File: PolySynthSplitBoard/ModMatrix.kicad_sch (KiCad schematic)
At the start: 89 parts, among them SW501 SB, SW502 MS1, SW503 MD1, SW504 MS2, SW505 MD2, SW506 MS3, SW507 MD3, SW508 MS4, SW509 MD4, SW510 MS5, SW511 MD5, SW512 MS6, SW513 MD6, SW514 MD7, SW515 MD8, U501 MCP23S17_SS

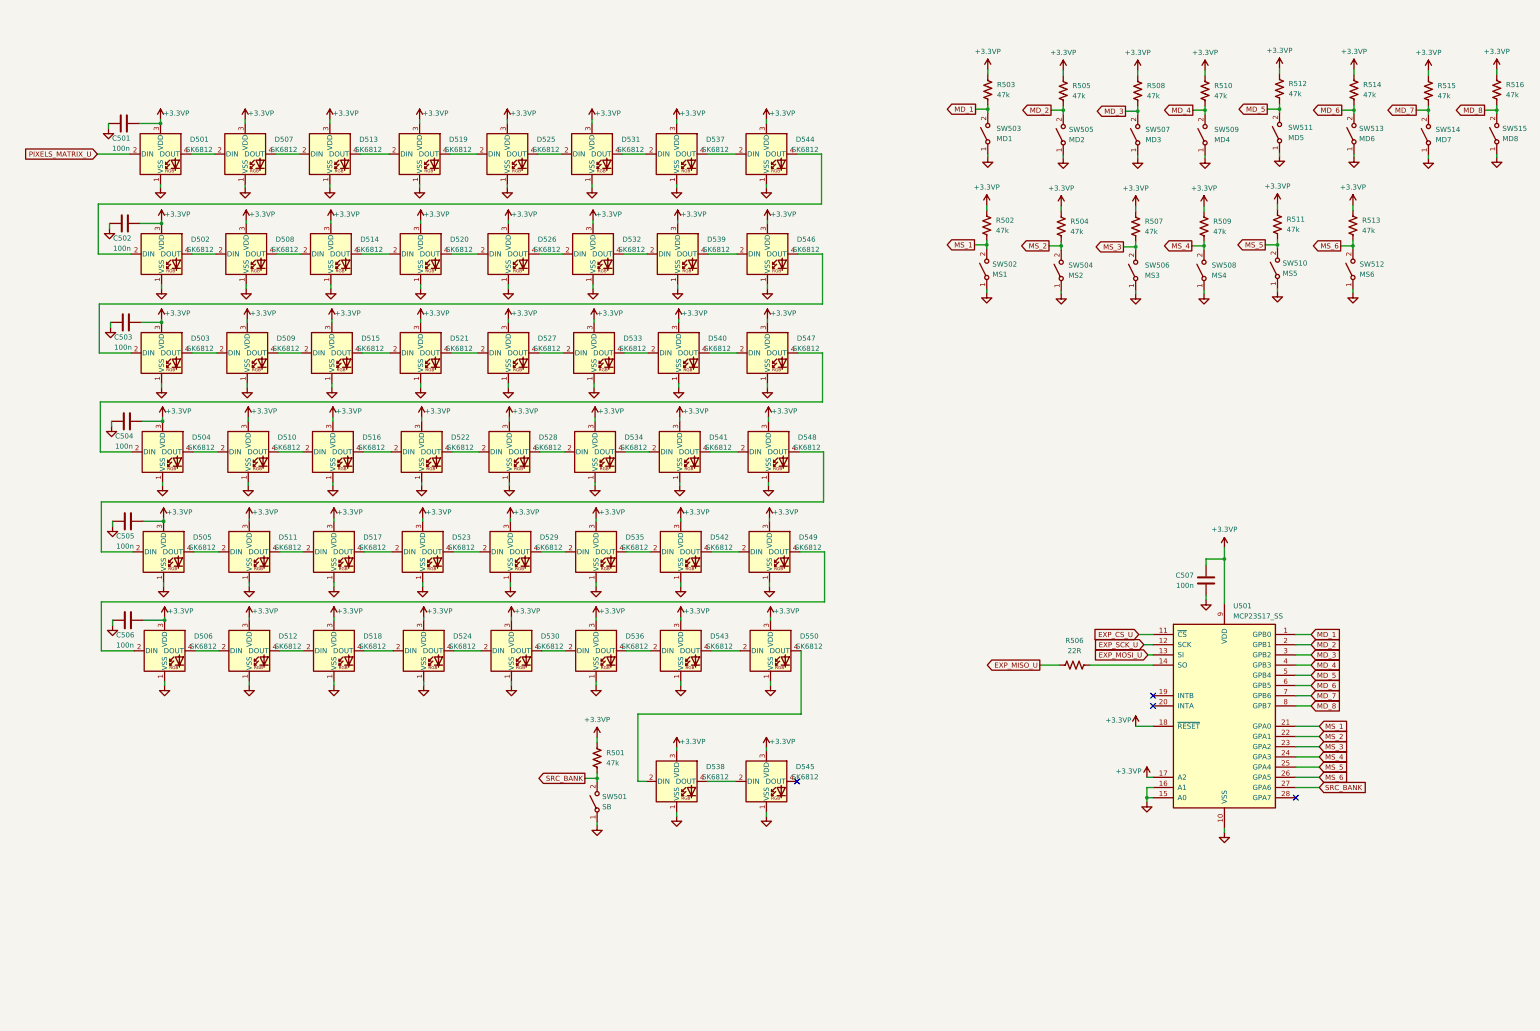
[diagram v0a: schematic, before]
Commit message: more decoupling on pixels, moved power connector
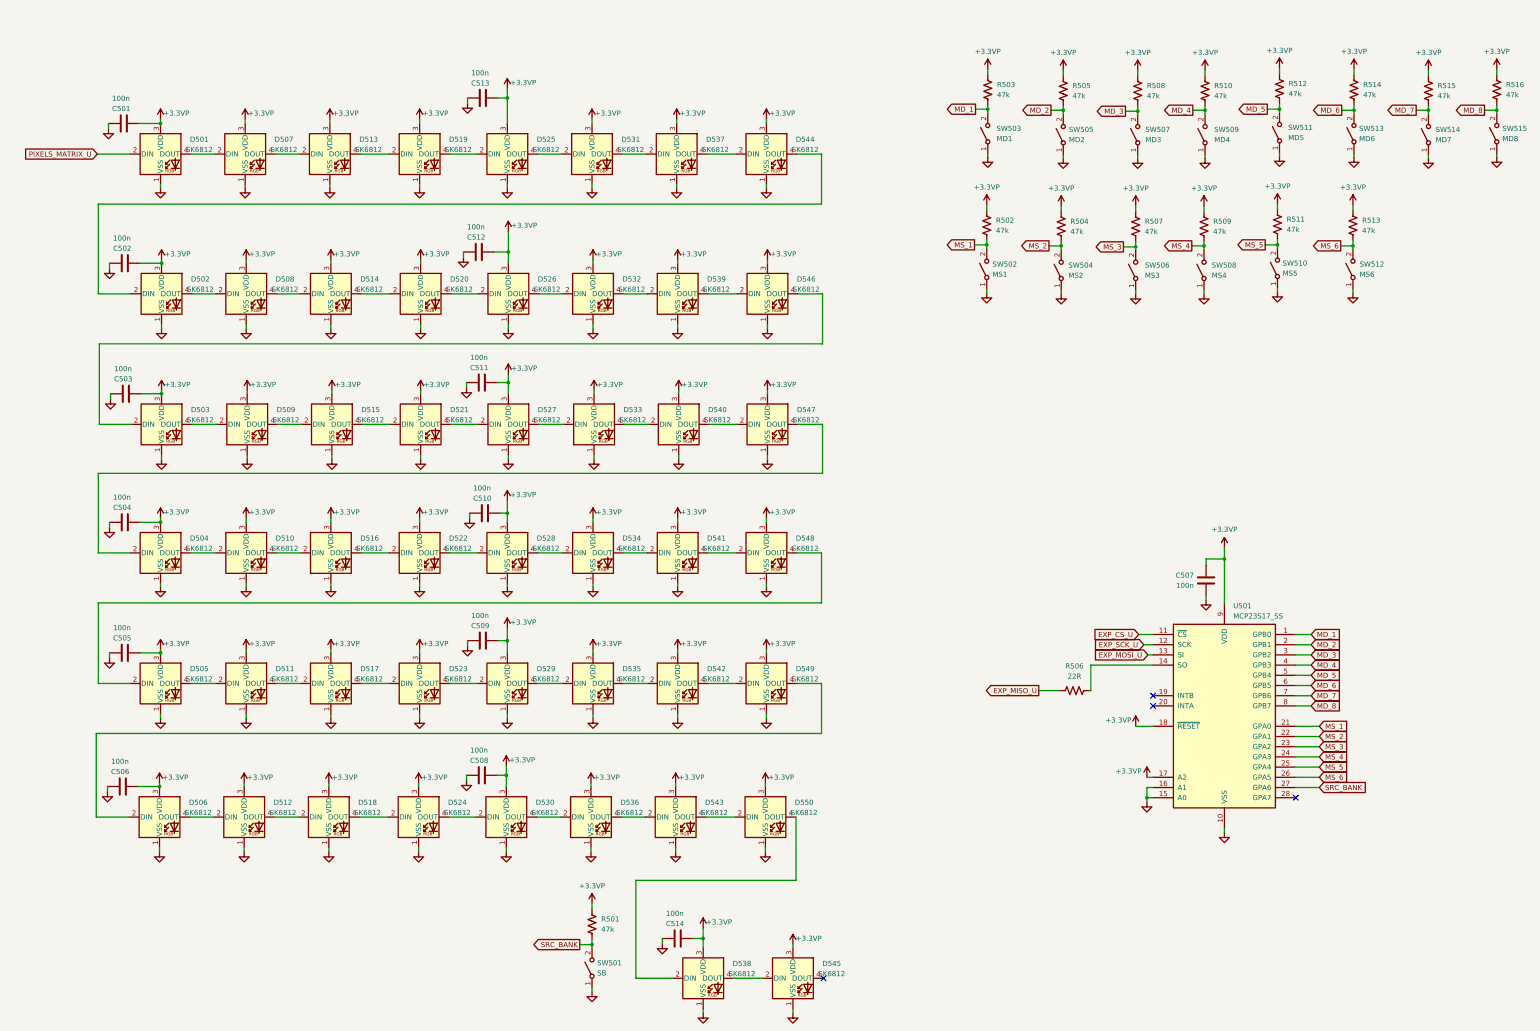
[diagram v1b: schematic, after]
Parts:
- added C508, C509, C510, C511, C512, C513, C514: 100n, Capacitor_SMD:C_0805_2012Metric, symbol Device:C
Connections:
- net +3.3VP: now also C508.2, C509.2, C510.2, C511.2, C512.2, C513.2, C514.2
- net GNDA: now also C508.1, C509.1, C510.1, C511.1, C512.1, C513.1, C514.1
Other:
- moved on the sheet: C502, C503, C504, C505, C506, D502, D503, D504, D505, D506, D508, D509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

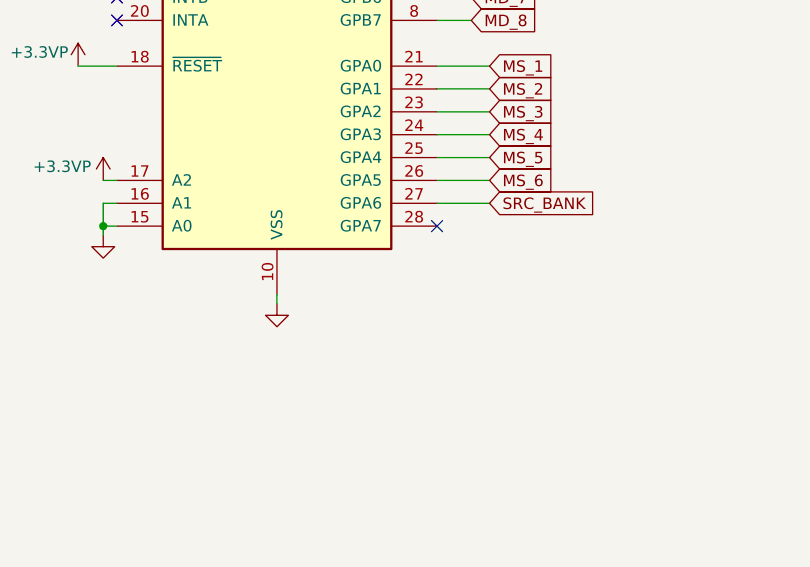
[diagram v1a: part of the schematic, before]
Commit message: Button indeces and mapping
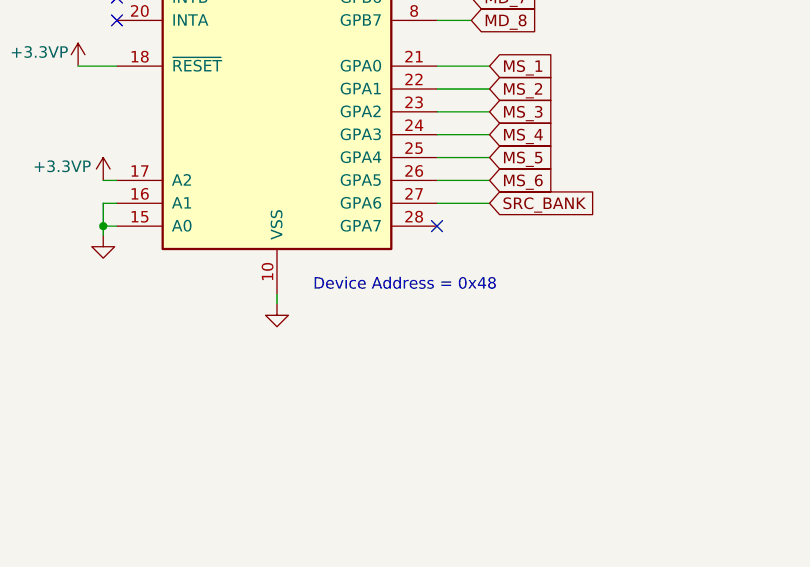
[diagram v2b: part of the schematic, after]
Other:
- note added: "Device Address = 0x48"
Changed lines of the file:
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@@
+		)
+	)
+	(text "Device Address = 0x48"
+		(exclude_from_sim no)
+		(at 335.788 223.52 0)
+		(effects
+			(font
+				(size 1.27 1.27)
+			)
 		)
 	)

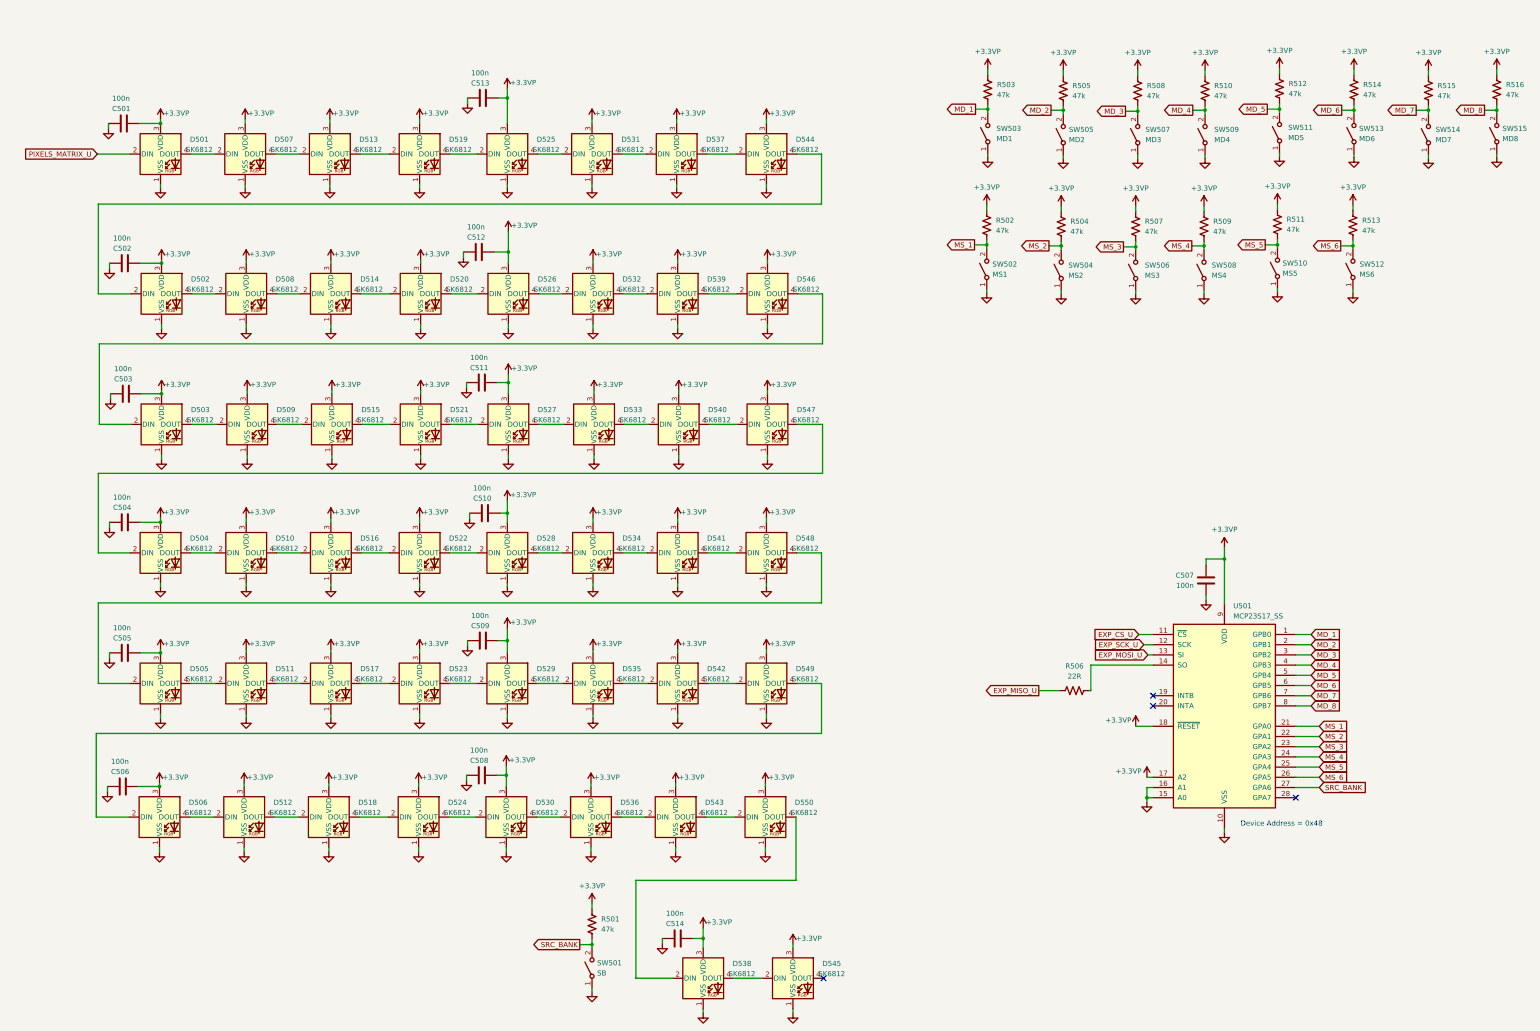
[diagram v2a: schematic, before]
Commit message: switching to 20p mezzanine connectors
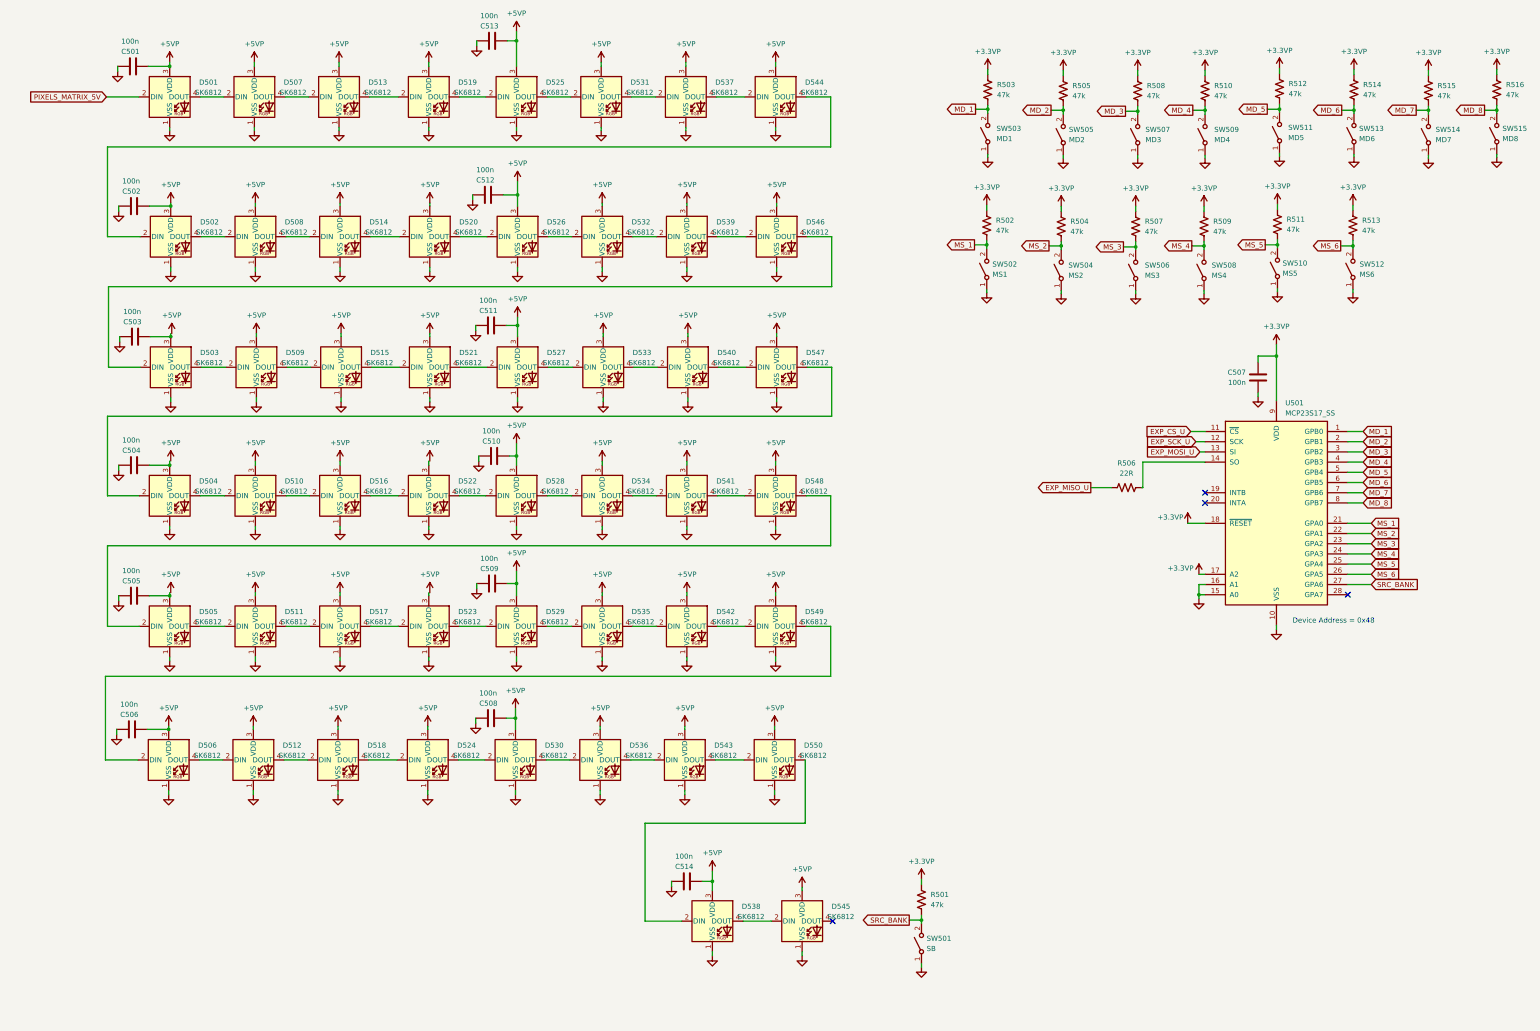
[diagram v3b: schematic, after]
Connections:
- net +3.3VP: no longer C501.2, C502.2, C503.2, C504.2, C505.2, C506.2, C508.2, C509.2, C510.2, C511.2, C512.2, C513.2, C514.2, D501.3 (VDD), D502.3 (VDD), D503.3 (VDD), D504.3 (VDD), D505.3 (VDD), D506.3 (VDD), D507.3 (VDD), D508.3 (VDD), D509.3 (VDD), D510.3 (VDD), D511.3 (VDD), D512.3 (VDD), D513.3 (VDD), D514.3 (VDD), D515.3 (VDD), D516.3 (VDD), D517.3 (VDD), D518.3 (VDD), D519.3 (VDD), D520.3 (VDD), D521.3 (VDD), D522.3 (VDD), D523.3 (VDD), D524.3 (VDD), D525.3 (VDD), D526.3 (VDD), D527.3 (VDD), D528.3 (VDD), D529.3 (VDD), D530.3 (VDD), D531.3 (VDD), D532.3 (VDD), D533.3 (VDD), D534.3 (VDD), D535.3 (VDD), D536.3 (VDD), D537.3 (VDD), D538.3 (VDD), D539.3 (VDD), D540.3 (VDD), D541.3 (VDD), D542.3 (VDD), D543.3 (VDD), D544.3 (VDD), D545.3 (VDD), D546.3 (VDD), D547.3 (VDD), D548.3 (VDD), D549.3 (VDD), D550.3 (VDD)
- net PIXELS_MATRIX_U renamed PIXELS_MATRIX_5V
- new net: C505.2, D505.3 (VDD)
- new net: C504.2, D504.3 (VDD)
- new net: C503.2, D503.3 (VDD)
- new net +5VP: C501.2, C502.2, C506.2, C508.2, C509.2, C510.2, C511.2, C512.2, C513.2, C514.2, D501.3 (VDD), D502.3 (VDD), D506.3 (VDD), D507.3 (VDD), D508.3 (VDD), D509.3 (VDD), D510.3 (VDD), D511.3 (VDD), D512.3 (VDD), D513.3 (VDD), D514.3 (VDD), D515.3 (VDD), D516.3 (VDD), D517.3 (VDD), D518.3 (VDD), D519.3 (VDD), D520.3 (VDD), D521.3 (VDD), D524.3 (VDD), D525.3 (VDD), D526.3 (VDD), D527.3 (VDD), D528.3 (VDD), D529.3 (VDD), D530.3 (VDD), D531.3 (VDD), D532.3 (VDD), D533.3 (VDD), D534.3 (VDD), D535.3 (VDD), D536.3 (VDD), D537.3 (VDD), D538.3 (VDD), D539.3 (VDD), D540.3 (VDD), D541.3 (VDD), D542.3 (VDD), D543.3 (VDD), D544.3 (VDD), D545.3 (VDD), D546.3 (VDD), D547.3 (VDD), D548.3 (VDD), D549.3 (VDD), D550.3 (VDD)
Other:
- moved on the sheet: C501, C502, C503, C504, C505, C506, C507, C508, C509, C510, C511, C512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

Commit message: motherboard rev2 passing DRC
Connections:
- net +5VP: now also C503.2, C504.2, C505.2, D503.3 (VDD), D504.3 (VDD), D505.3 (VDD), D522.3 (VDD), D523.3 (VDD)
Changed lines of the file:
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@@
 	(wire
 		(pts
-			(xy 58.928 165.862) (xy 58.928 166.624)
+			(xy 58.928 165.1) (xy 58.928 166.624)
 		)
 		(stroke
@@
 	(symbol
 		(lib_id "power:+5VP")
-		(at 59.436 101.346 0)
+		(at 59.182 101.346 0)
 		(unit 1)
 		(exclude_from_sim no)
@@
 		(fields_autoplaced yes)
 		(property "Reference" "#PWR0544"
-			(at 59.436 105.156 0)
+			(at 59.182 105.156 0)
 			(effects
 				(font
@@
 		)
 		(property "Value" "+5VP"
-			(at 59.436 96.774 0)
+			(at 59.182 96.774 0)
 			(effects
 				(font
@@
 		)
 		(property "Footprint" ""
-			(at 59.436 101.346 0)
+			(at 59.182 101.346 0)
 			(effects
 				(font
@@
 		)
 		(property "Datasheet" ""
-			(at 59.436 101.346 0)
+			(at 59.182 101.346 0)
 			(effects
 				(font
@@
 		)
 		(property "Description" "Power symbol creates a global label with name \"+5VP\""
-			(at 59.436 101.346 0)
+			(at 59.182 101.346 0)
 			(effects
 				(font
@@
 	(symbol
 		(lib_id "power:+5VP")
-		(at 123.698 133.096 0)
+		(at 123.444 133.096 0)
 		(unit 1)
 		(exclude_from_sim no)
@@
 		(fields_autoplaced yes)
 		(property "Reference" "#PWR0566"
-			(at 123.698 136.906 0)
+			(at 123.444 136.906 0)
 			(effects
 				(font
@@
 		)
 		(property "Value" "+5VP"
-			(at 123.698 128.524 0)
+			(at 123.444 128.524 0)
 			(effects
 				(font
@@
 		)
 		(property "Footprint" ""
-			(at 123.698 133.096 0)
+			(at 123.444 133.096 0)
 			(effects
 				(font
@@
 		)
 		(property "Datasheet" ""
-			(at 123.698 133.096 0)
+			(at 123.444 133.096 0)
 			(effects
 				(font
@@
 		)
 		(property "Description" "Power symbol creates a global label with name \"+5VP\""
-			(at 123.698 133.096 0)
+			(at 123.444 133.096 0)
 			(effects
 				(font
@@
 	(symbol
 		(lib_id "power:+5VP")
-		(at 59.182 133.096 0)
+		(at 58.928 133.096 0)
 		(unit 1)
 		(exclude_from_sim no)
@@
 		(fields_autoplaced yes)
 		(property "Reference" "#PWR0560"
-			(at 59.182 136.906 0)
+			(at 58.928 136.906 0)
 			(effects
 				(font
@@
 		)
 		(property "Value" "+5VP"
-			(at 59.182 128.524 0)
+			(at 58.928 128.524 0)
 			(effects
 				(font
@@
 		)
 		(property "Footprint" ""
-			(at 59.182 133.096 0)
+			(at 58.928 133.096 0)
 			(effects
 				(font
@@
 		)
 		(property "Datasheet" ""
-			(at 59.182 133.096 0)
+			(at 58.928 133.096 0)
 			(effects
 				(font
@@
 		)
 		(property "Description" "Power symbol creates a global label with name \"+5VP\""
-			(at 59.182 133.096 0)
+			(at 58.928 133.096 0)
 			(effects
 				(font
@@
 	(symbol
 		(lib_id "power:+5VP")
-		(at 123.698 165.862 0)
+		(at 123.444 165.862 0)
 		(unit 1)
 		(exclude_from_sim no)
@@
 		(fields_autoplaced yes)
 		(property "Reference" "#PWR0582"
-			(at 123.698 169.672 0)
+			(at 123.444 169.672 0)
 			(effects
 				(font
@@
 		)
 		(property "Value" "+5VP"
-			(at 123.698 161.29 0)
+			(at 123.444 161.29 0)
 			(effects
 				(font
@@
 		)
 		(property "Footprint" ""
-			(at 123.698 165.862 0)
+			(at 123.444 165.862 0)
 			(effects
 				(font
@@
 		)
 		(property "Datasheet" ""
-			(at 123.698 165.862 0)
+			(at 123.444 165.862 0)
 			(effects
 				(font
@@
 		)
 		(property "Description" "Power symbol creates a global label with name \"+5VP\""
-			(at 123.698 165.862 0)
+			(at 123.444 165.862 0)
 			(effects
 				(font
@@
 	(symbol
 		(lib_id "power:+5VP")
-		(at 59.182 165.862 0)
+		(at 58.928 165.1 0)
 		(unit 1)
 		(exclude_from_sim no)
@@
 		(fields_autoplaced yes)
 		(property "Reference" "#PWR0576"
-			(at 59.182 169.672 0)
+			(at 58.928 168.91 0)
 			(effects
 				(font
@@
 		)
 		(property "Value" "+5VP"
-			(at 59.182 161.29 0)
+			(at 58.928 160.528 0)
 			(effects
 				(font
@@
 		)
 		(property "Footprint" ""
-			(at 59.182 165.862 0)
+			(at 58.928 165.1 0)
 			(effects
 				(font
@@
 		)
 		(property "Datasheet" ""
-			(at 59.182 165.862 0)
+			(at 58.928 165.1 0)
 			(effects
 				(font
@@
 		)
 		(property "Description" "Power symbol creates a global label with name \"+5VP\""
-			(at 59.182 165.862 0)
+			(at 58.928 165.1 0)
 			(effects
 				(font
